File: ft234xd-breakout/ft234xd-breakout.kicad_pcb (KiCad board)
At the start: 2 copper layers, 12.7 x 17.8 mm, 20 parts, among them CON1 USB-MINI-B, P1 CONN_5, P2 CONN_5, U1 FT234XD

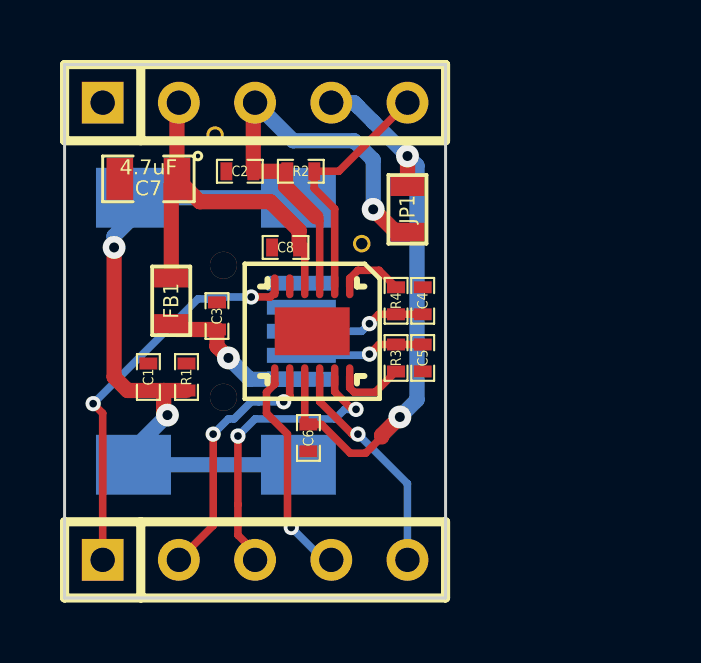
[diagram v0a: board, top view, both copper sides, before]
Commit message: fixed dfn12 pad spacing
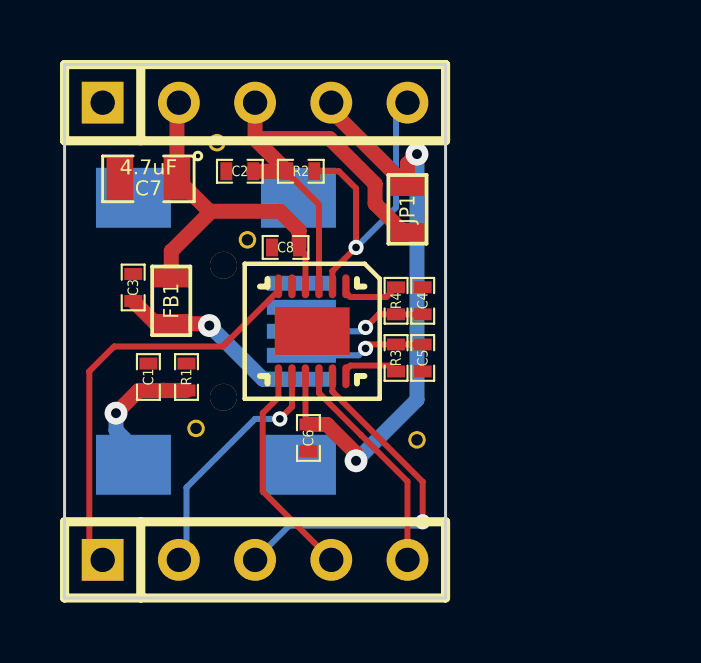
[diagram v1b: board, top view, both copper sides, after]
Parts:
- removed the Hole at (194.2, 74.7)
- added Hole: VAL**, Hole, F.Cu at (193.6, 84.5)
- added Hole: VAL**, Hole, F.Cu at (201.0, 84.9)
- added Hole: VAL**, Hole, F.Cu at (195.3, 78.2)
- moved Hole 5.88 mm to (194.3, 75.0)
- moved C3 2.95 mm to (191.5, 79.8)
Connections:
- CON1 pad 6: N-0000011 -> (no net)
- CON1 pad 8: N-0000011 -> (no net)
- CON1 pad 9: N-0000011 -> (no net)
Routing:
- net N-0000011: track 22.8 -> 4.62 mm, vias 2 -> 1
- net RESET: track 8.17 -> 10.8 mm, vias 0 -> 1
- net CTS: track 10.3 -> 12.2 mm, vias 2 -> 1
- net N-000001: track 5.44 -> 6.69 mm
- net VCCIO: track 18.9 -> 20.0 mm
- net CBUS0: track 13.1 -> 14.0 mm, vias 2 -> 0
- net 3V3OUT: track 15.5 -> 14.9 mm, vias 1 -> 0
- net VBUS: track 12.7 -> 12.1 mm
- net RTS: track 8.40 -> 8.17 mm, vias 2 -> 1
- net RXD: track 7.44 -> 7.34 mm, vias 1 -> 0
- net TXD: track 7.28 -> 7.29 mm, vias 1 -> 0
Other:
- net class Default: trace_width 0.1524 -> 0.2
- net class Power: trace_width 0.508 -> 0.5
- net class Signal: trace_width 0.254 -> 0.2

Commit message: simplified and shrunk ft234xd board
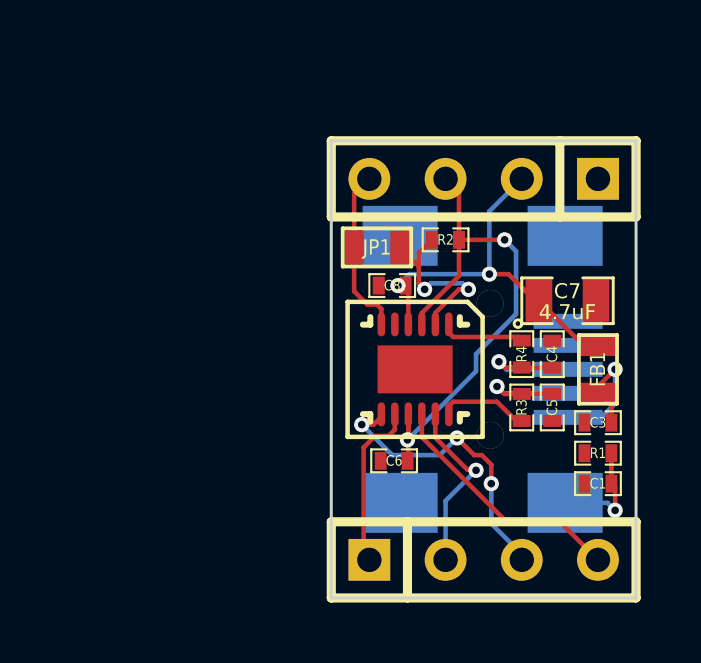
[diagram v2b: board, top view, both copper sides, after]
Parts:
- removed C2: 0.1uF, SM0402_c
- removed Hole (x4): VAL**, Hole
- P1, P2: value CONN_5 -> CONN_4; footprint SIL-5 -> SIL-4
- moved C3 16.1 mm to (207.0, 84.3), turned to 180 degrees
- moved C1 15.4 mm to (207.0, 86.4), turned to 180 degrees
- moved C7 14.5 mm to (206.0, 80.3), turned to 0 degrees
- moved FB1 14.4 mm to (207.0, 82.5)
- moved R1 13.9 mm to (207.0, 85.3), turned to 180 degrees
- moved CON1 8.98 mm to (202.6, 82.5)
- moved P1 6.84 mm to (203.2, 76.2), turned to 180 degrees
- moved P2 6.35 mm to (203.2, 88.9)
- moved R2 5.34 mm to (201.9, 78.2), turned to 0 degrees
- moved C4 4.67 mm to (205.5, 82.0)
- moved C5 4.62 mm to (205.5, 83.8)
- moved R4 4.55 mm to (204.5, 82.0)
- moved R3 4.50 mm to (204.5, 83.8)
- moved C8 3.78 mm to (200.2, 79.8)
- moved U1 3.66 mm to (200.9, 82.5)
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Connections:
- C1 pad 1: N-0000011 -> N-000005
- C6 pad 1: VCCIO -> 3V3OUT
- CON1 pad 6: (no net) -> N-000005
- CON1 pad 7: N-0000011 -> (no net)
- JP1 pad 1: 3V3OUT -> RESET
- JP1 pad 2: VCCIO -> CBUS0
- P1 pad 4: VCCIO -> CBUS0
- P2 pad 1: CBUS0 -> RTS
- P2 pad 2: RTS -> CTS
- P2 pad 3: CTS -> TXD
- P2 pad 4: TXD -> RXD
- R1 pad 1: N-0000011 -> N-000005
- U1 pad 9: VCCIO -> 3V3OUT
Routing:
- net VCCIO: track 20.0 -> 0.00 mm, vias 2 -> 0
- net CBUS0: track 14.0 -> 5.62 mm
- net CTS: track 12.2 -> 5.99 mm
- net N-0000011: track 4.62 -> 0.00 mm, vias 1 -> 0
- net RESET: track 10.8 -> 6.25 mm, vias 1 -> 2
- net N-000005: track 0.00 -> 3.72 mm, vias 0 -> 1
- net 3V3OUT: track 14.9 -> 17.8 mm, vias 0 -> 2
- net RTS: track 8.17 -> 5.62 mm, vias 1 -> 0
- net TXD: track 7.29 -> 9.78 mm, vias 0 -> 3
- net N-000007: track 6.69 -> 5.10 mm
- net D+: track 2.02 -> 3.03 mm
- net RXD: track 7.34 -> 8.32 mm
- net VBUS: track 12.1 -> 13.0 mm, vias 0 -> 2
- net D-: track 2.07 -> 2.82 mm
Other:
- board size 12.7 x 17.8 mm -> 10.2 x 15.2 mm
- net class Default: trace_width 0.2 -> 0.1524
- net class Power: trace_width 0.5 -> 0.2032
- net class Signal: trace_width 0.2 -> 0.2032
